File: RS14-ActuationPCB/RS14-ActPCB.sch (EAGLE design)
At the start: 34 parts, among them IC1 L293D, IC2 L293D, P12V 22-23-2021, T1 2N3904, T2 2N3904, T3 2N3904, T4 2N3904

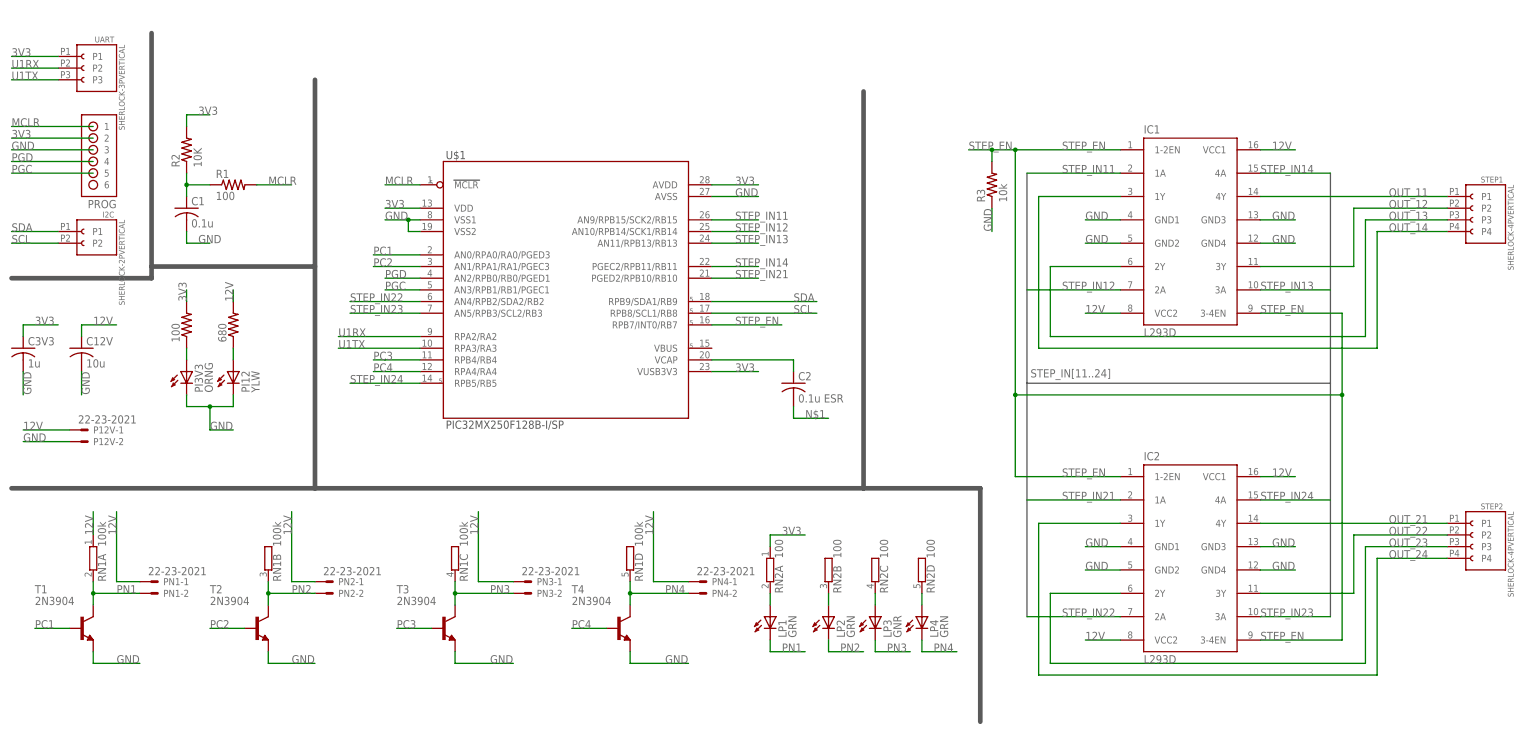
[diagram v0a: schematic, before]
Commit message: Updated Actuation PCB
This is the first draft layout.

It only has two of the four desired screw holes, but this is mainly due
to my refusal to make the board bigger in my tired stubbornness. There
is also no labeling on the board (other than small built in markers) as
of yet. So this will need to be added as well.
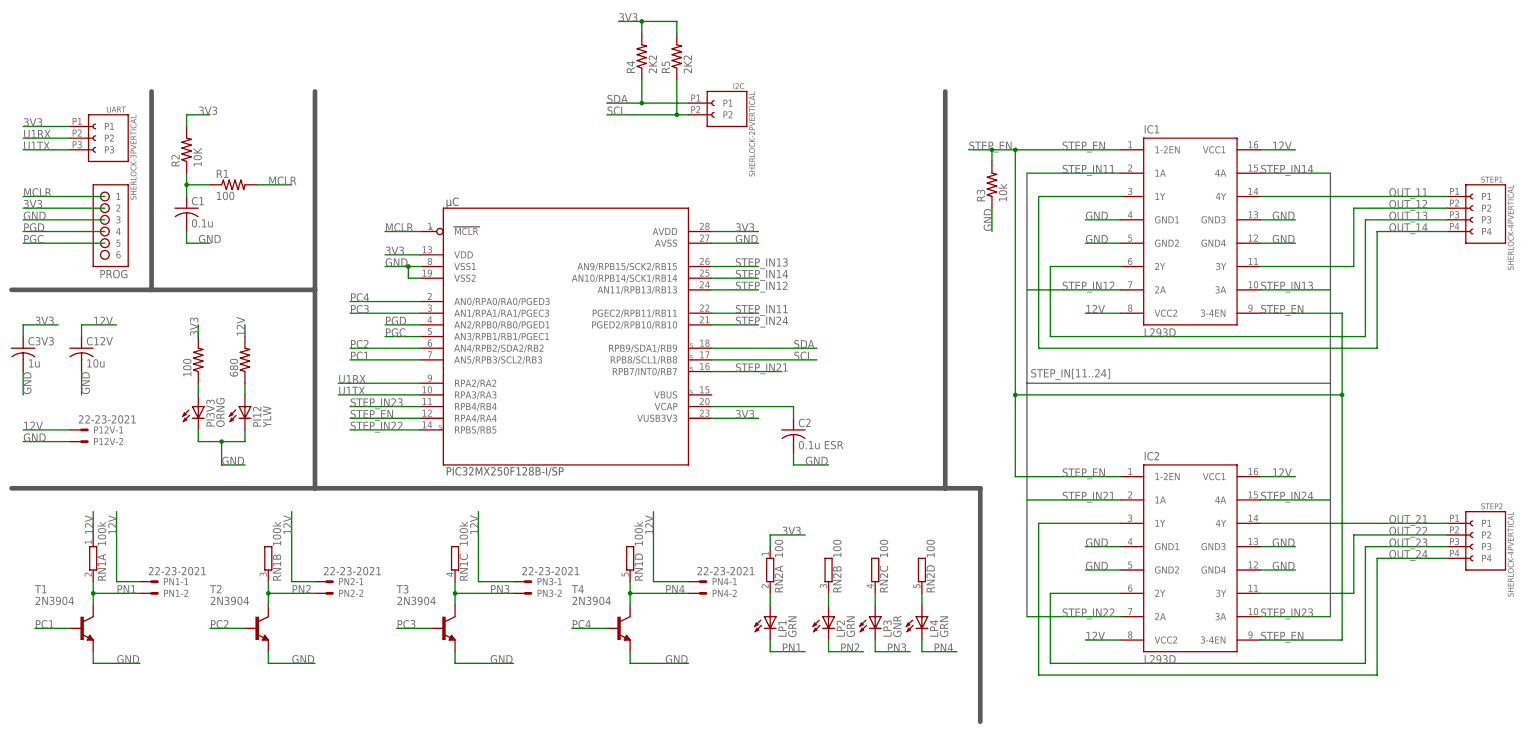
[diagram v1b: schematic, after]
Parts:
- removed U$1: PIC32MX250F128B-I/SP, Microchip_By_element14_Batch_1:PIC32MX250F128B-I/SP
- added R4, R5: 2K2, rcl:R-US_0204/7
- added µC: PIC32MX250F128B-I/SP, Microchip_By_element14_Batch_1:PIC32MX250F128B-I/SP
- 100, 680, R1, R2, R3: device rcl:R-US_0207/15 -> rcl:R-US_0204/7
- C12V: device rcl:C-US025-025X050 -> rcl:C-US025-060X050
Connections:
- removed net N$1: C2.2
- net 3V3: now also R4.2, R5.2, µC.AVDD, µC.VDD, µC.VUSB3V3; no longer U$1.AVDD, U$1.VDD, U$1.VUSB3V3
- net GND: now also C2.2, µC.AVSS, µC.VSS1, µC.VSS2; no longer U$1.AVSS, U$1.VSS1, U$1.VSS2
- net MCLR: now also µC.MCLR; no longer U$1.MCLR
- net N$2: now also µC.VCAP; no longer U$1.VCAP
- net PC1: now also µC.AN5/RPB3/SCL2/RB3; no longer U$1.AN0/RPA0/RA0/PGED3
- net PC2: now also µC.AN4/RPB2/SDA2/RB2; no longer U$1.AN1/RPA1/RA1/PGEC3
- net PC3: now also µC.AN1/RPA1/RA1/PGEC3; no longer U$1.RPB4/RB4
- net PC4: now also µC.AN0/RPA0/RA0/PGED3; no longer U$1.RPA4/RA4
- net PGC: now also µC.AN3/RPB1/RB1/PGEC1; no longer U$1.AN3/RPB1/RB1/PGEC1
- net PGD: now also µC.AN2/RPB0/RB0/PGED1; no longer U$1.AN2/RPB0/RB0/PGED1
- net SCL: now also R5.1, µC.RPB8/SCL1/RB8; no longer U$1.RPB8/SCL1/RB8
- net SDA: now also R4.1, µC.RPB9/SDA1/RB9; no longer U$1.RPB9/SDA1/RB9
- net STEP_EN: now also µC.RPA4/RA4; no longer U$1.RPB7/INT0/RB7
- net STEP_IN11: now also µC.PGEC2/RPB11/RB11; no longer U$1.AN9/RPB15/SCK2/RB15
- net STEP_IN12: now also µC.AN11/RPB13/RB13; no longer U$1.AN10/RPB14/SCK1/RB14
- net STEP_IN13: now also µC.AN9/RPB15/SCK2/RB15; no longer U$1.AN11/RPB13/RB13
- net STEP_IN14: now also µC.AN10/RPB14/SCK1/RB14; no longer U$1.PGEC2/RPB11/RB11
- net STEP_IN21: now also µC.RPB7/INT0/RB7; no longer U$1.PGED2/RPB10/RB10
- net STEP_IN22: now also µC.RPB5/RB5; no longer U$1.AN4/RPB2/SDA2/RB2
- net STEP_IN23: now also µC.RPB4/RB4; no longer U$1.AN5/RPB3/SCL2/RB3
- net STEP_IN24: now also µC.PGED2/RPB10/RB10; no longer U$1.RPB5/RB5
- net U1RX: now also µC.RPA2/RA2; no longer U$1.RPA2/RA2
- net U1TX: now also µC.RPA3/RA3; no longer U$1.RPA3/RA3
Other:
- moved on the sheet: 100, 680, C2, I2C, PI12, PI3V3, PROG, UART

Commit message: Updated ActPCB with mounting holes and labels
This includes larger print labels next to each pneumatic to identify which number of the pneumatic is being used, as well as large pring STEP1 and STEP2 next to each header to make them more visible.
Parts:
- I2C: value SHERLOCK-2PVERTICAL -> SHERLOCK-3PVERTICAL; device rs-molex-sherlock:SHERLOCK-2PVERTICAL -> rs-molex-sherlock:SHERLOCK-3PVERTICAL
- R12V: value (none) -> 680
- R3V3: value (none) -> 100
- renumbered 100 to R3V3, 680 to R12V
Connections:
- net 3V3: now also I2C.P1
- net SCL: now also I2C.P3; no longer I2C.P2
- net SDA: now also I2C.P2; no longer I2C.P1
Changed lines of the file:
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@@
 <part name="R1" library="rcl" deviceset="R-US_" device="0204/7" value="100"/>
 <part name="R2" library="rcl" deviceset="R-US_" device="0204/7" value="10K"/>
-<part name="100" library="rcl" deviceset="R-US_" device="0204/7"/>
-<part name="680" library="rcl" deviceset="R-US_" device="0204/7"/>
+<part name="R3V3" library="rcl" deviceset="R-US_" device="0204/7" value="100"/>
+<part name="R12V" library="rcl" deviceset="R-US_" device="0204/7" value="680"/>
 <part name="IC1" library="st-microelectronics" deviceset="L293D" device=""/>
 <part name="IC2" library="st-microelectronics" deviceset="L293D" device=""/>
@@
 <part name="PN4" library="con-molex" deviceset="22-23-2021" device=""/>
 <part name="PROG" library="rs-extra-cons" deviceset="HDR-1X6-OFFSET" device=""/>
-<part name="I2C" library="rs-molex-sherlock" deviceset="SHERLOCK-2P" device="VERTICAL"/>
+<part name="I2C" library="rs-molex-sherlock" deviceset="SHERLOCK-3P" device="VERTICAL"/>
 <part name="UART" library="rs-molex-sherlock" deviceset="SHERLOCK-3P" device="VERTICAL"/>
 <part name="STEP1" library="rs-molex-sherlock" deviceset="SHERLOCK-4P" device="VERTICAL"/>
@@
 <instance part="R1" gate="G$1" x="35.56" y="78.74"/>
 <instance part="R2" gate="G$1" x="25.4" y="86.36" rot="R90"/>
-<instance part="100" gate="G$1" x="27.94" y="40.64" rot="R90"/>
-<instance part="680" gate="G$1" x="38.1" y="40.64" rot="R90"/>
+<instance part="R3V3" gate="G$1" x="27.94" y="40.64" rot="R90"/>
+<instance part="R12V" gate="G$1" x="38.1" y="40.64" rot="R90"/>
 <instance part="IC1" gate="G$1" x="243.84" y="68.58"/>
 <instance part="IC2" gate="G$1" x="243.84" y="-2.54"/>
@@
 <instance part="PN4" gate="-2" x="137.16" y="-10.16"/>
 <instance part="PROG" gate="G$1" x="7.62" y="60.96" rot="MR0"/>
-<instance part="I2C" gate="G$1" x="139.7" y="93.98" rot="MR0"/>
+<instance part="I2C" gate="G$1" x="142.24" y="96.52" rot="MR0"/>
 <instance part="UART" gate="G$1" x="5.08" y="88.9" rot="MR0"/>
 <instance part="STEP1" gate="G$1" x="304.8" y="73.66" rot="MR0"/>
@@
 </segment>
 <segment>
-<pinref part="100" gate="G$1" pin="2"/>
+<pinref part="R3V3" gate="G$1" pin="2"/>
 <wire x1="27.94" y1="45.72" x2="27.94" y2="48.26" width="0.1524" layer="91"/>
 <label x="27.94" y="45.72" size="1.778" layer="95" rot="R90"/>
@@
 <junction x="124.46" y="114.3"/>
 <label x="119.38" y="114.3" size="1.778" layer="95"/>
+<pinref part="I2C" gate="G$1" pin="P1"/>
+<wire x1="137.16" y1="99.06" x2="137.16" y2="114.3" width="0.1524" layer="91"/>
+<wire x1="137.16" y1="114.3" x2="132.08" y2="114.3" width="0.1524" layer="91"/>
+<junction x="132.08" y="114.3"/>
 </segment>
 </net>
@@
 <net name="N$5" class="0">
 <segment>
-<pinref part="680" gate="G$1" pin="1"/>
+<pinref part="R12V" gate="G$1" pin="1"/>
 <pinref part="PI12" gate="G$1" pin="A"/>
 <wire x1="38.1" y1="35.56" x2="38.1" y2="33.02" width="0.1524" layer="91"/>
@@
 <net name="N$7" class="0">
 <segment>
-<pinref part="100" gate="G$1" pin="1"/>
+<pinref part="R3V3" gate="G$1" pin="1"/>
 <pinref part="PI3V3" gate="G$1" pin="A"/>
 <wire x1="27.94" y1="35.56" x2="27.94" y2="33.02" width="0.1524" layer="91"/>
@@
 </segment>
 <segment>
-<pinref part="680" gate="G$1" pin="2"/>
+<pinref part="R12V" gate="G$1" pin="2"/>
 <wire x1="38.1" y1="45.72" x2="38.1" y2="48.26" width="0.1524" layer="91"/>
 <label x="38.1" y="45.72" size="1.778" layer="95" rot="R90"/>
@@
 </segment>
 <segment>
-<wire x1="134.62" y1="96.52" x2="124.46" y2="96.52" width="0.1524" layer="91"/>
 <label x="116.84" y="96.52" size="1.778" layer="95"/>
-<pinref part="I2C" gate="G$1" pin="P1"/>
 <pinref part="R4" gate="G$1" pin="1"/>
 <wire x1="124.46" y1="96.52" x2="116.84" y2="96.52" width="0.1524" layer="91"/>
 <wire x1="124.46" y1="101.6" x2="124.46" y2="96.52" width="0.1524" layer="91"/>
+<pinref part="I2C" gate="G$1" pin="P2"/>
+<wire x1="124.46" y1="96.52" x2="137.16" y2="96.52" width="0.1524" layer="91"/>
 <junction x="124.46" y="96.52"/>
 </segment>
@@
 </segment>
 <segment>
-<wire x1="134.62" y1="93.98" x2="132.08" y2="93.98" width="0.1524" layer="91"/>
 <label x="116.84" y="93.98" size="1.778" layer="95"/>
-<pinref part="I2C" gate="G$1" pin="P2"/>
 <pinref part="R5" gate="G$1" pin="1"/>
 <wire x1="132.08" y1="93.98" x2="116.84" y2="93.98" width="0.1524" layer="91"/>
 <wire x1="132.08" y1="101.6" x2="132.08" y2="93.98" width="0.1524" layer="91"/>
+<pinref part="I2C" gate="G$1" pin="P3"/>
+<wire x1="137.16" y1="93.98" x2="132.08" y2="93.98" width="0.1524" layer="91"/>
 <junction x="132.08" y="93.98"/>
 </segment>

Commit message: Battery Lockout PCB Added
This commit adds the current version of the Battery Lockout/Power Controller PCB to our design. It also includes revisions to the main actuation PCB to change the LEDs to the 3mm convention we addopted.
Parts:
- PI12, PI3V3: device led:LED5MM -> led:LED3MM
- µC: value PIC32MX250F128B-I/SP -> PIC32MX250F128B
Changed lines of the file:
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@@
 <layer number="48" name="Document" color="7" fill="1" visible="no" active="no"/>
 <layer number="49" name="Reference" color="7" fill="1" visible="no" active="no"/>
+<layer number="50" name="dxf" color="7" fill="1" visible="no" active="no"/>
 <layer number="51" name="tDocu" color="7" fill="1" visible="no" active="no"/>
 <layer number="52" name="bDocu" color="7" fill="1" visible="no" active="no"/>
+<layer number="53" name="tGND_GNDA" color="7" fill="9" visible="no" active="no"/>
+<layer number="54" name="bGND_GNDA" color="1" fill="9" visible="no" active="no"/>
+<layer number="56" name="wert" color="7" fill="1" visible="no" active="no"/>
 <layer number="91" name="Nets" color="2" fill="1" visible="yes" active="yes"/>
 <layer number="92" name="Busses" color="1" fill="1" visible="yes" active="yes"/>
@@
 <layer number="98" name="Guide" color="6" fill="1" visible="yes" active="yes"/>
 <layer number="100" name="Image" color="15" fill="10" visible="yes" active="yes"/>
+<layer number="101" name="Patch_Top" color="12" fill="4" visible="yes" active="yes"/>
+<layer number="102" name="Vscore" color="7" fill="1" visible="yes" active="yes"/>
+<layer number="103" name="tMap" color="7" fill="1" visible="yes" active="yes"/>
+<layer number="104" name="Name" color="16" fill="1" visible="yes" active="yes"/>
+<layer number="105" name="tPlate" color="7" fill="1" visible="yes" active="yes"/>
+<layer number="106" name="bPlate" color="7" fill="1" visible="yes" active="yes"/>
+<layer number="107" name="Crop" color="7" fill="1" visible="yes" active="yes"/>
+<layer number="116" name="Patch_BOT" color="9" fill="4" visible="yes" active="yes"/>
+<layer number="121" name="_tsilk" color="7" fill="1" visible="yes" active="yes"/>
+<layer number="122" name="_bsilk" color="7" fill="1" visible="yes" active="yes"/>
+<layer number="125" name="_tNames" color="7" fill="1" visible="yes" active="yes"/>
+<layer number="144" name="Drill_legend" color="7" fill="1" visible="yes" active="yes"/>
+<layer number="151" name="HeatSink" color="7" fill="1" visible="yes" active="yes"/>
 <layer number="200" name="200bmp" color="1" fill="10" visible="yes" active="yes"/>
 <layer number="201" name="bmp" color="2" fill="1" visible="yes" active="yes"/>
+<layer number="202" name="202bmp" color="3" fill="10" visible="yes" active="yes"/>
+<layer number="203" name="203bmp" color="4" fill="10" visible="yes" active="yes"/>
+<layer number="204" name="204bmp" color="5" fill="10" visible="yes" active="yes"/>
+<layer number="205" name="205bmp" color="6" fill="10" visible="yes" active="yes"/>
+<layer number="206" name="206bmp" color="7" fill="10" visible="yes" active="yes"/>
+<layer number="207" name="207bmp" color="8" fill="10" visible="yes" active="yes"/>
+<layer number="208" name="208bmp" color="9" fill="10" visible="yes" active="yes"/>
+<layer number="209" name="209bmp" color="7" fill="1" visible="yes" active="yes"/>
+<layer number="210" name="210bmp" color="7" fill="1" visible="yes" active="yes"/>
+<layer number="211" name="211bmp" color="7" fill="1" visible="yes" active="yes"/>
+<layer number="212" name="212bmp" color="7" fill="1" visible="yes" active="yes"/>
+<layer number="213" name="213bmp" color="7" fill="1" visible="yes" active="yes"/>
+<layer number="214" name="214bmp" color="7" fill="1" visible="yes" active="yes"/>
+<layer number="215" name="215bmp" color="7" fill="1" visible="yes" active="yes"/>
+<layer number="216" name="216bmp" color="7" fill="1" visible="yes" active="yes"/>
+<layer number="217" name="217bmp" color="18" fill="1" visible="no" active="no"/>
+<layer number="218" name="218bmp" color="19" fill="1" visible="no" active="no"/>
+<layer number="219" name="219bmp" color="20" fill="1" visible="no" active="no"/>
+<layer number="220" name="220bmp" color="21" fill="1" visible="no" active="no"/>
+<layer number="221" name="221bmp" color="22" fill="1" visible="no" active="no"/>
+<layer number="222" name="222bmp" color="23" fill="1" visible="no" active="no"/>
+<layer number="223" name="223bmp" color="24" fill="1" visible="no" active="no"/>
+<layer number="224" name="224bmp" color="25" fill="1" visible="no" active="no"/>
+<layer number="250" name="Descript" color="3" fill="1" visible="no" active="no"/>
+<layer number="251" name="SMDround" color="12" fill="11" visible="no" active="no"/>
+<layer number="254" name="cooling" color="7" fill="1" visible="yes" active="yes"/>
 </layers>
 <schematic xreflabel="%F%N/%S.%C%R" xrefpart="/%S.%C%R">
@@
 </classes>
 <parts>
-<part name="µC" library="Microchip_By_element14_Batch_1" deviceset="PIC32MX250F128B-I/SP" device=""/>
+<part name="µC" library="Microchip_By_element14_Batch_1" deviceset="PIC32MX250F128B-I/SP" device="" value="PIC32MX250F128B"/>
 <part name="C1" library="rcl" deviceset="C-US" device="025-025X050" value="0.1u"/>
 <part name="R1" library="rcl" deviceset="R-US_" device="0204/7" value="100"/>
@@
 <part name="IC1" library="st-microelectronics" deviceset="L293D" device=""/>
 <part name="IC2" library="st-microelectronics" deviceset="L293D" device=""/>
-<part name="PI12" library="led" deviceset="LED" device="5MM" value="YLW"/>
-<part name="PI3V3" library="led" deviceset="LED" device="5MM" value="ORNG"/>
+<part name="PI12" library="led" deviceset="LED" device="3MM" value="YLW"/>
+<part name="PI3V3" library="led" deviceset="LED" device="3MM" value="ORNG"/>
 <part name="T1" library="transistor" deviceset="2N3904" device=""/>
 <part name="T2" library="transistor" deviceset="2N3904" device=""/>

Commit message: Updated layouts for new hole sizes
Updated both boards to include proper sized holes for the screws (correction from 0.22" radius to 0.22" diamater clearance). This also includes some minor tweeks to clean up the board size a bit.
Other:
- note added: "Each line here, is rated at 200mA"
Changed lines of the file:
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@@
 <part name="PROG" library="rs-extra-cons" deviceset="HDR-1X6-OFFSET" device=""/>
 <part name="I2C" library="rs-molex-sherlock" deviceset="SHERLOCK-3P" device="VERTICAL"/>
-<part name="UART" library="rs-molex-sherlock" deviceset="SHERLOCK-3P" device="VERTICAL"/>
 <part name="STEP1" library="rs-molex-sherlock" deviceset="SHERLOCK-4P" device="VERTICAL"/>
 <part name="STEP2" library="rs-molex-sherlock" deviceset="SHERLOCK-4P" device="VERTICAL"/>
@@
 <part name="R4" library="rcl" deviceset="R-US_" device="0204/7" value="2K2"/>
 <part name="R5" library="rcl" deviceset="R-US_" device="0204/7" value="2K2"/>
+<part name="UART" library="rs-molex-sherlock" deviceset="SHERLOCK-3P" device="VERTICAL"/>
 </parts>
 <sheets>
@@
 <wire x1="53.34" y1="12.7" x2="53.34" y2="55.88" width="1.016" layer="97"/>
 <wire x1="53.34" y1="55.88" x2="53.34" y2="99.06" width="1.016" layer="97"/>
+<frame x1="-17.78" y1="-50.8" x2="325.12" y2="121.92" columns="8" rows="5" layer="94"/>
+<text x="287.02" y="30.48" size="2.032" layer="97">Each line here,
+is rated at 200mA</text>
+<text x="73.66" y="-38.1" size="2.032" layer="97">Each line here,
+is rated at 200mA</text>
 </plain>
 <instances>
@@
 <instance part="PROG" gate="G$1" x="7.62" y="60.96" rot="MR0"/>
 <instance part="I2C" gate="G$1" x="142.24" y="96.52" rot="MR0"/>
-<instance part="UART" gate="G$1" x="5.08" y="88.9" rot="MR0"/>
 <instance part="STEP1" gate="G$1" x="304.8" y="73.66" rot="MR0"/>
 <instance part="STEP2" gate="G$1" x="304.8" y="2.54" rot="MR0"/>
@@
 <instance part="R4" gate="G$1" x="124.46" y="106.68" rot="R90"/>
 <instance part="R5" gate="G$1" x="132.08" y="106.68" rot="R90"/>
+<instance part="UART" gate="G$1" x="5.08" y="88.9" rot="MR0"/>
 </instances>
 <busses>
@@
 </schematic>
 </drawing>
+<compatibility>
+<note version="6.3" minversion="6.2.2" severity="warning">
+Since Version 6.2.2 text objects can contain more than one line,
+which will not be processed correctly with this version.
+</note>
+</compatibility>
 </eagle>
